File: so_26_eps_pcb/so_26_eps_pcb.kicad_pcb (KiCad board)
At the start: 4 copper layers, 90.2 x 95.9 mm, 47 parts, among them J1 Conn_02x12_Odd_Even, J3 Conn_01x02, SW1 SW_SPDT, U1 LM22679TJ-ADJ/NOPB, U2 LM22679TJ-ADJ/NOPB

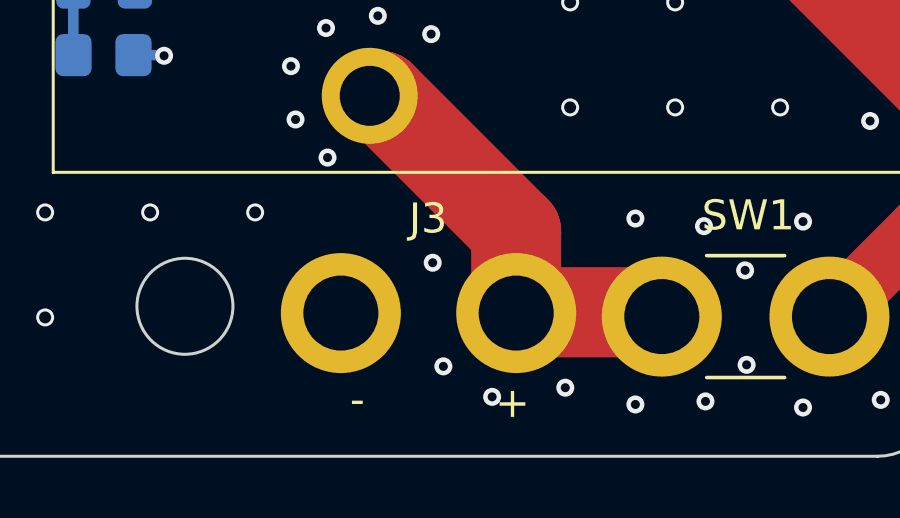
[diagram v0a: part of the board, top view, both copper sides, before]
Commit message: added text "ext pwr 10-16.8v"
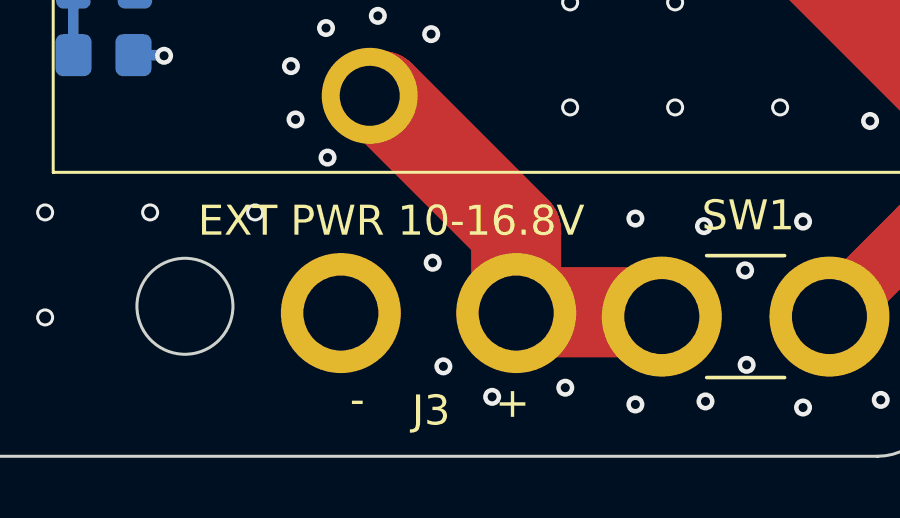
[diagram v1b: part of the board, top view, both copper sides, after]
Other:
- board text added: "EXT PWR 10-16.8V"
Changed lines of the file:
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@@
 		(at 81.574 120.8985 180)
 		(property "Reference" "J3"
-			(at -0.1124 9.6283 0)
+			(at -0.214 3.2275 0)
 			(unlocked yes)
 			(layer "F.SilkS")
@@
 		(layer "Edge.Cuts")
 	)
+	(gr_text "EXT PWR 10-16.8V"
+		(at 74.0156 111.9306 0)
+		(layer "F.SilkS")
+		(effects
+			(font
+				(size 1 1)
+				(thickness 0.15)
+			)
+			(justify left bottom)
+		)
+	)
 	(gr_text "+3V3"

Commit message: added rev 1 text
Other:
- board text added: "SO26 - EPS REV 1 KATHARINA NILSSEN 11.02.26"
- board text removed: "SO26 - EPS KATHARINA NILSSEN 11.02.26"
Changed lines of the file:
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@@
 		)
 	)
-	(gr_text "SO26 - EPS\nKATHARINA NILSSEN\n11.02.26"
-		(at 70.866 33.1398 90)
+	(gr_text "SO26 - EPS\nREV 1\nKATHARINA NILSSEN\n11.02.26"
+		(at 71.9328 32.8858 90)
 		(layer "B.SilkS")
 		(effects

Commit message: added text
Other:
- board text added: "+ POLES HERE"
- board text added: "- POLES HERE"
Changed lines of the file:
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@@
 		(layer "Edge.Cuts")
 	)
+	(gr_text "+ POLES HERE"
+		(at 68.2752 109.9494 90)
+		(layer "F.SilkS" knockout)
+		(effects
+			(font
+				(size 2 2)
+				(thickness 0.15)
+			)
+			(justify left bottom)
+		)
+	)
+	(gr_text "- POLES HERE"
+		(at 68.2752 54.2218 90)
+		(layer "F.SilkS" knockout)
+		(effects
+			(font
+				(size 2 2)
+				(thickness 0.15)
+			)
+			(justify left bottom)
+		)
+	)
 	(gr_text "EXT PWR 10-16.8V"
-		(at 74.0156 111.9306 0)
-		(layer "F.SilkS")
+		(at 72.1868 111.6766 0)
+		(layer "F.SilkS" knockout)
 		(effects
 			(font
@@
 	(gr_text "+3V3"
 		(at 77.937123 105.3948 0)
-		(layer "B.SilkS")
+		(layer "B.SilkS" knockout)
 		(effects
 			(font
@@
 	(gr_text "+10V"
 		(at 87.2236 32.9366 90)
-		(layer "B.SilkS")
+		(layer "B.SilkS" knockout)
 		(effects
 			(font
@@
 	(gr_text "+3V3"
 		(at 117.1956 39.5914 0)
-		(layer "B.SilkS")
+		(layer "B.SilkS" knockout)
 		(effects
 			(font
@@
 	(gr_text "VBAT_1"
 		(at 133.7056 31.9206 90)
-		(layer "B.SilkS")
+		(layer "B.SilkS" knockout)
 		(effects
 			(font
@@
 	(gr_text "ALT_+10V"
 		(at 94.2848 31.0062 90)
-		(layer "B.SilkS")
+		(layer "B.SilkS" knockout)
 		(effects
 			(font
@@
 	(gr_text "+10V"
 		(at 77.937123 85.8702 0)
-		(layer "B.SilkS")
+		(layer "B.SilkS" knockout)
 		(effects
 			(font
@@
 	(gr_text "VBAT_0"
 		(at 123.5456 31.819 90)
-		(layer "B.SilkS")
+		(layer "B.SilkS" knockout)
 		(effects
 			(font
@@
 	(gr_text "ALT_+10V"
 		(at 81.1276 96.1826 0)
-		(layer "B.SilkS")
+		(layer "B.SilkS" knockout)
 		(effects
 			(font

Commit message: Placed components for 10V
Also made a filled zone for VBAT
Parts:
- removed 18650 BATTERY HOLDER: ~, Myfootprints:Battery holder
- added CELL_1: ~, Myfootprints:Battery holder, F.Cu at (79.8, 106.4)
- F1, SW1: moved to B.Cu
- moved D4 158.3 mm to (221.2, 53.9)
- moved D6 157.3 mm to (221.2, 47.8)
- moved D5 153.9 mm to (221.2, 50.8)
- moved SW1 149.6 mm to (225.9, 53.1), turned to 0 degrees
- moved R12 135.3 mm to (203.3, 113.7)
- moved R13 133.2 mm to (203.3, 110.7)
- moved R11 132.9 mm to (203.3, 116.6)
- moved R9 127.8 mm to (214.2, 52.9), turned to 0 degrees
- moved R10 121.0 mm to (214.2, 48.0), turned to 0 degrees
- moved R2 109.8 mm to (198.5, 119.6), turned to 0 degrees
- moved R1 109.4 mm to (198.5, 122.5), turned to 0 degrees
- moved C9 102.0 mm to (230.6, 53.9), turned to 0 degrees
- moved D3 96.7 mm to (199.9, 96.2), turned to 0 degrees
- moved C11 95.5 mm to (191.0, 120.1), turned to 0 degrees
- moved F1 91.1 mm to (203.9, 54.6)
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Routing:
- net VBAT: track 110.6 -> 0.00 mm, vias 17 -> 0
- net +3V3: track 103.5 -> 0.00 mm, vias 2 -> 0
- net Net-(CELL_1-Pad6): track 92.0 -> 0.00 mm
- net Net-(CELL_1-Pad2): track 83.9 -> 0.00 mm
- net Net-(CELL_1-Pad4): track 83.6 -> 0.00 mm
- net +10V_ALT: track 73.1 -> 0.00 mm, vias 1 -> 0
- net +10V: track 54.9 -> 0.00 mm
- net GND: track 53.9 -> 0.00 mm, vias 297 -> 0
- net Net-(SW1-B): track 34.0 -> 0.00 mm
- net /VBAT_1: track 22.3 -> 0.00 mm
- net /VBAT_0: track 20.8 -> 0.00 mm
- net Net-(J3-Pin_1): track 14.7 -> 0.00 mm
- net Net-(JP1-C): track 9.90 -> 0.00 mm
- net Net-(U2-FB): track 8.34 -> 0.00 mm
- net Net-(U1-FB): track 8.32 -> 0.00 mm
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- removed copper zone on B.Cu, net +10V
- removed copper zone on B.Cu, net +10V_ALT
- removed copper zone on B.Cu, net +3V3
- removed copper zone on B.Cu, net GND
- removed copper zone on F.Cu, net GND
- removed copper zone on B.Cu, net Net-(D1-K)
- removed copper zone on B.Cu, net Net-(D2-K)
- removed copper zone on B.Cu, net REG_+10V
- removed copper zone on B.Cu, net REG_+3V3
- removed copper zone on F.Cu, net VBAT

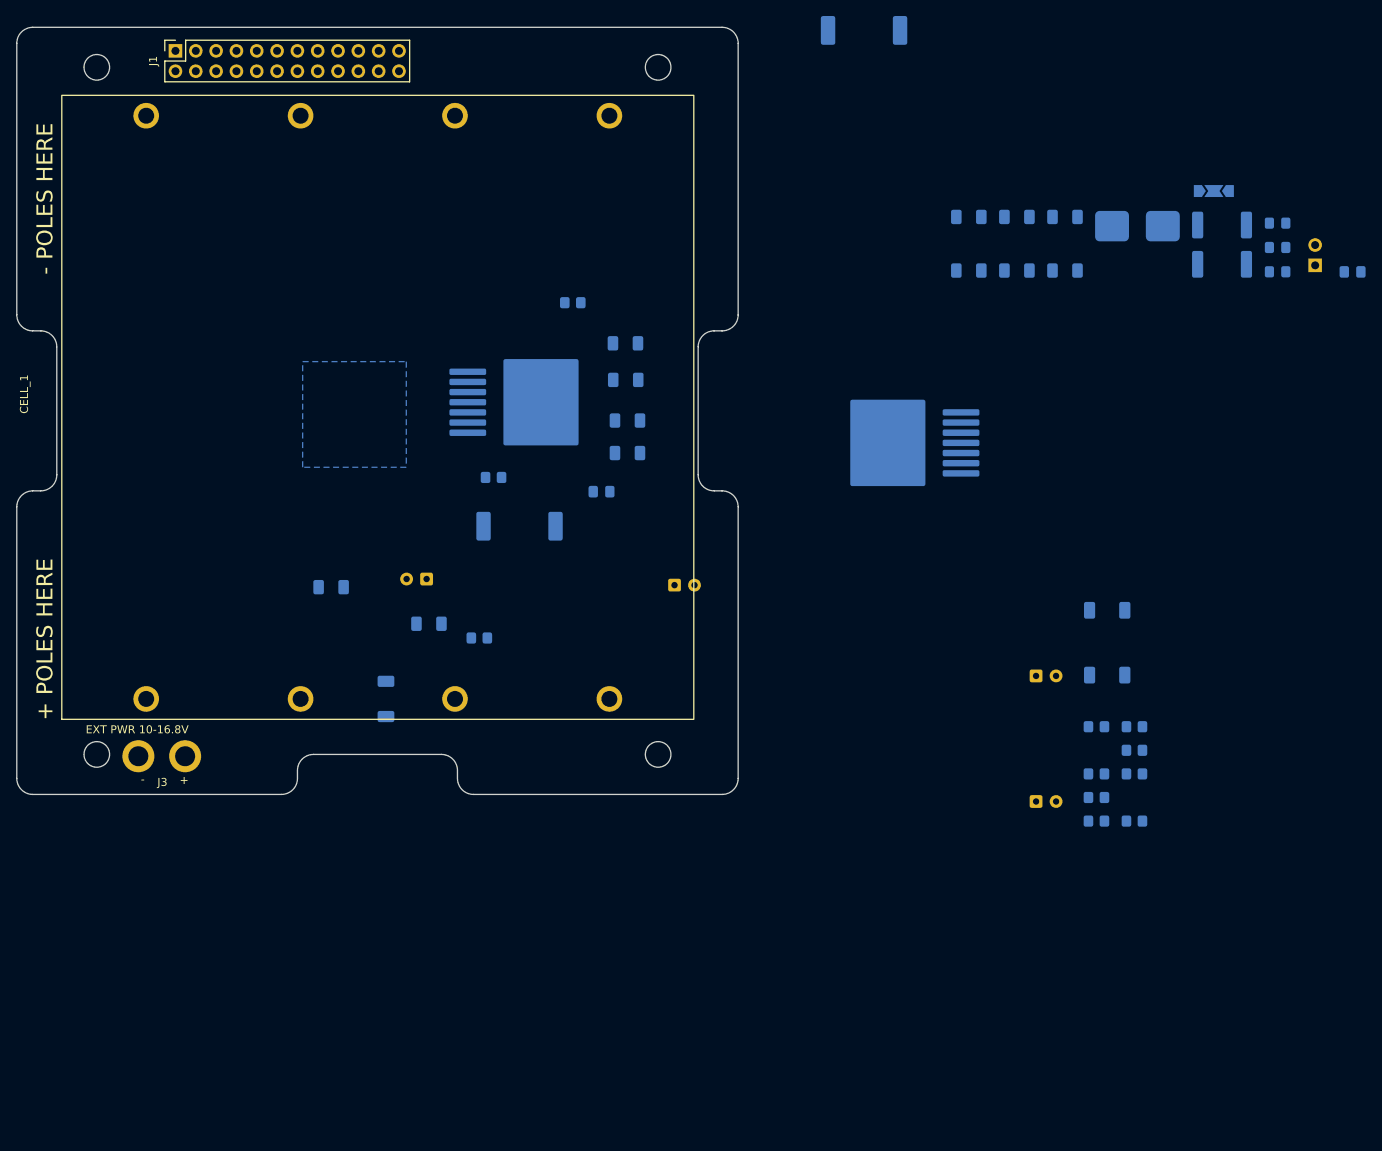
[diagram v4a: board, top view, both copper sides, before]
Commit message: Placed VBAT components and wiring
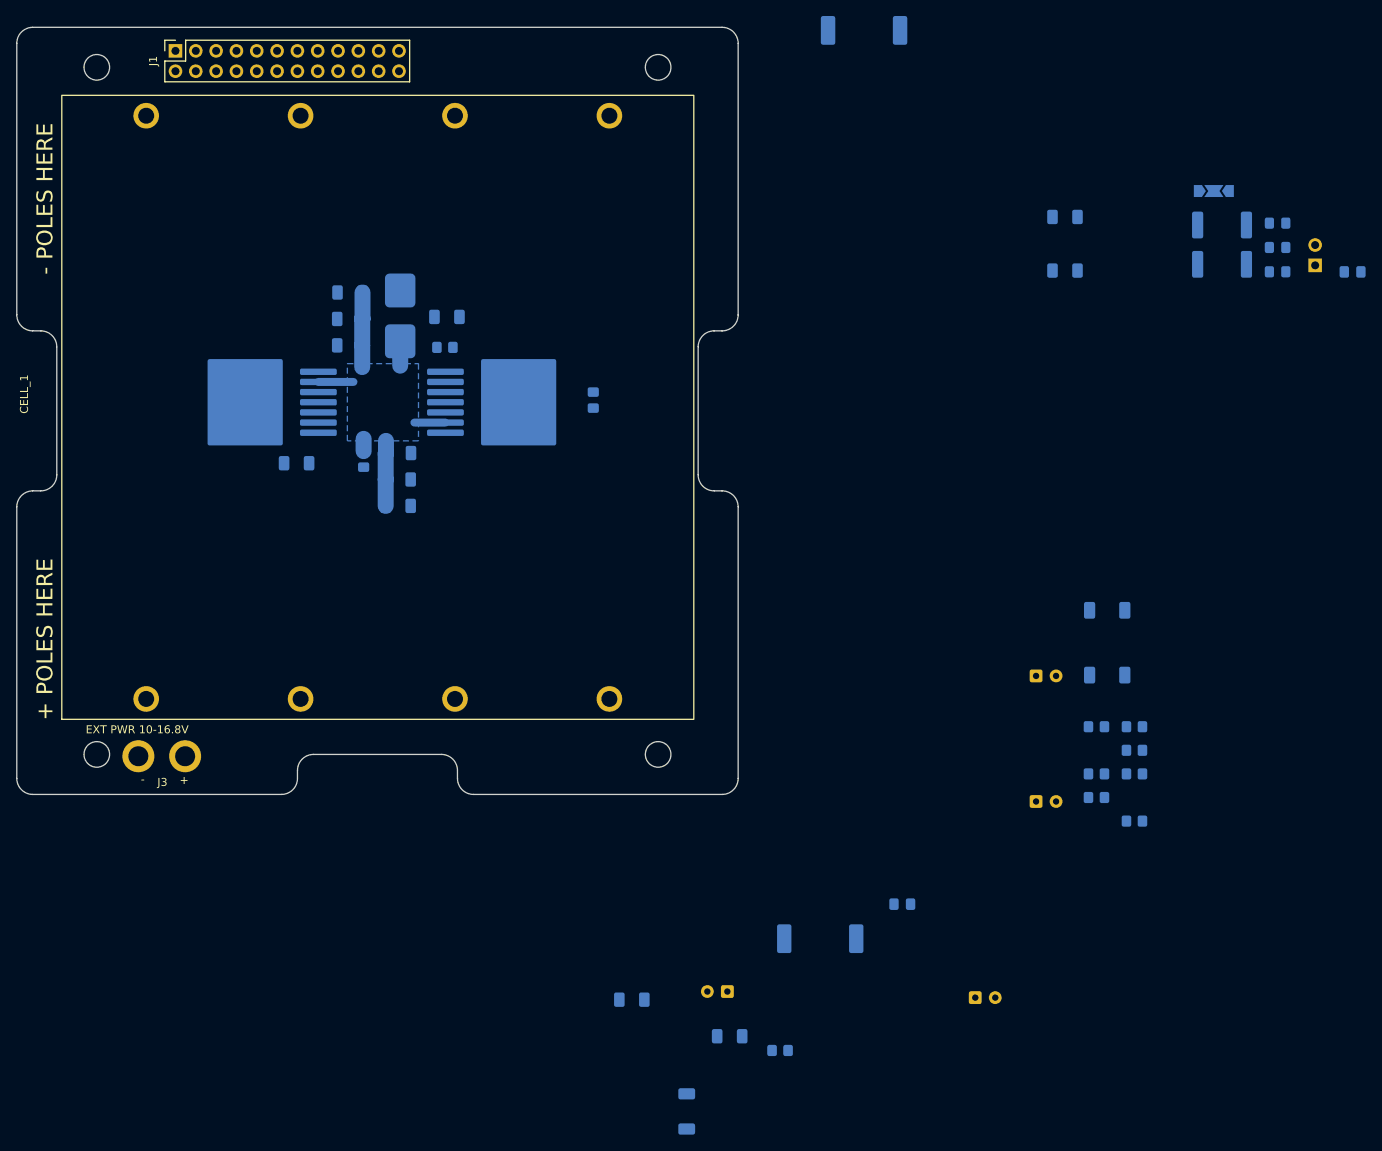
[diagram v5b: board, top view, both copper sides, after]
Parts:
- moved R1 102.2 mm to (106.9, 77.3), turned to -90 degrees
- moved F1 99.0 mm to (105.0, 59.6), turned to -90 degrees
- moved C7 95.2 mm to (98.6, 77.8), turned to 180 degrees
- moved C5 80.6 mm to (111.3, 76.5), turned to 180 degrees
- moved U1 80.5 mm to (93.6, 70.2)
- moved C3 78.5 mm to (111.3, 79.8), turned to 180 degrees
- moved C1 77.2 mm to (111.3, 83.1), turned to 180 degrees
- moved C10 63.8 mm to (174.3, 132.9)
- moved C12 63.8 mm to (183.4, 144.6)
- moved C14 63.8 mm to (152.4, 143.8)
- moved C18 63.8 mm to (152.7, 149.4)
- moved R6 63.8 mm to (159.0, 151.2)
- moved D2 63.8 mm to (147.3, 158.8)
- moved L2 63.8 mm to (164.1, 143.3)
- moved C16 63.8 mm to (140.5, 144.8)
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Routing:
- net VBAT: track 0.00 -> 30.3 mm
